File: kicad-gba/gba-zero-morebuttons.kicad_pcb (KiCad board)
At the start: 2 copper layers, 130.7 x 72.9 mm, 71 parts, among them J1 SWTCHCRFT_3.5JACK5-JACK-SMD, P1 50_PIN_CON, P3 LINK_CONNECTOR, Q1 BSS138, U1 APX803, U2 NC7WZ16, U3 74LVC2G02, U4 74LVC3G04, U5 LM4875, U6 RPI-ZEROSMD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

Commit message: fixed major issue
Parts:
- removed REF**: Val**, gba-zero-morebuttons:XY_BUTTON
- added S7: XY_BUTTON, gba-zero-morebuttons:XY_BUTTON, F.Cu at (200.1, 97.6)
- P2: value (none) -> JST_2PIN
- S5: value Val** -> AB_BUTTON
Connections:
- net AUD_PWM renamed /AUD_PWM
- net BAT renamed Net-(P2-2)
- net BKLT renamed /BKLT
- net BKLT_PWM renamed /BKLT_PWM
- net BTN_A renamed /BTN_A
- net BTN_B renamed /BTN_B
- net BTN_D renamed /BTN_D
- net BTN_L renamed /BTN_L
- net BTN_LS renamed /BTN_LS
- net BTN_R renamed /BTN_R
- net BTN_RS renamed /BTN_RS
- net BTN_SEL renamed /BTN_SEL
- net BTN_STR renamed /BTN_STR
- net BTN_U renamed /BTN_U
- net BYPASS renamed Net-(C10-P$1)
- net LBO renamed /LBO
- net MISO renamed /MISO
- net MOSI renamed /MOSI
- net MOSI_3V renamed /MOSI_3V
- net PWR_EN_RPI renamed /PWR_EN_RPI
- net PWR_SW_SEN renamed /PWR_SW_SEN
- net RING renamed Net-(C13-P$2)
- net RT_INT renamed /RT_INT
- net RXD renamed /RXD
- net SCL renamed /SCL
- net SCLK renamed /SCLK
- net SCLK_3V renamed /SCLK_3V
- net SDA renamed /SDA
- net SENSE renamed Net-(U5-SENSE)
- net TFT_CS_3V renamed /TFT_CS_3V
- net TFT_DC_3V renamed /TFT_DC_3V
- net TFT_RST renamed /TFT_RST
- net TXD renamed /TXD
- net USB renamed /USB
- net VO1 renamed Net-(C13-P$1)
- net VO2 renamed Net-(SP1--)
- net VOL/SD renamed Net-(U5-VOL/~{SD})
- J1 pad 4: (no net) -> unconnected-(J1-Pad4)
- P1 pad 11: (no net) -> unconnected-(P1-VSYNC-Pad11)
- P1 pad 12: (no net) -> unconnected-(P1-HSYNC-Pad12)
- P1 pad 13: (no net) -> unconnected-(P1-DOTCLK-Pad13)
- P1 pad 14: (no net) -> unconnected-(P1-DE-Pad14)
- P1 pad 35: (no net) -> unconnected-(P1-/RD-Pad35)
- P1 pad 39: (no net) -> unconnected-(P1-TE-Pad39)
- R17 pad 2O: (no net) -> unconnected-(R17-Pad2O)
- U2 pad 3: (no net) -> unconnected-(U2-A2-Pad3)
- U2 pad 4: (no net) -> unconnected-(U2-Y2-Pad4)
- U6 pad 31: (no net) -> /BTN_X
- U6 pad 35: (no net) -> /BTN_Y
- U7 pad VS: (no net) -> unconnected-(U7-PadVS)
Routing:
- net (no net): track 78.7 -> 0.00 mm, vias 2 -> 0
- net /BTN_X: track 0.00 -> 43.5 mm, vias 0 -> 1
- net /BTN_Y: track 0.00 -> 42.4 mm, vias 0 -> 1
- net BTN_Y: track 3.77 -> 0.00 mm
- net BTN_X: track 3.73 -> 0.00 mm

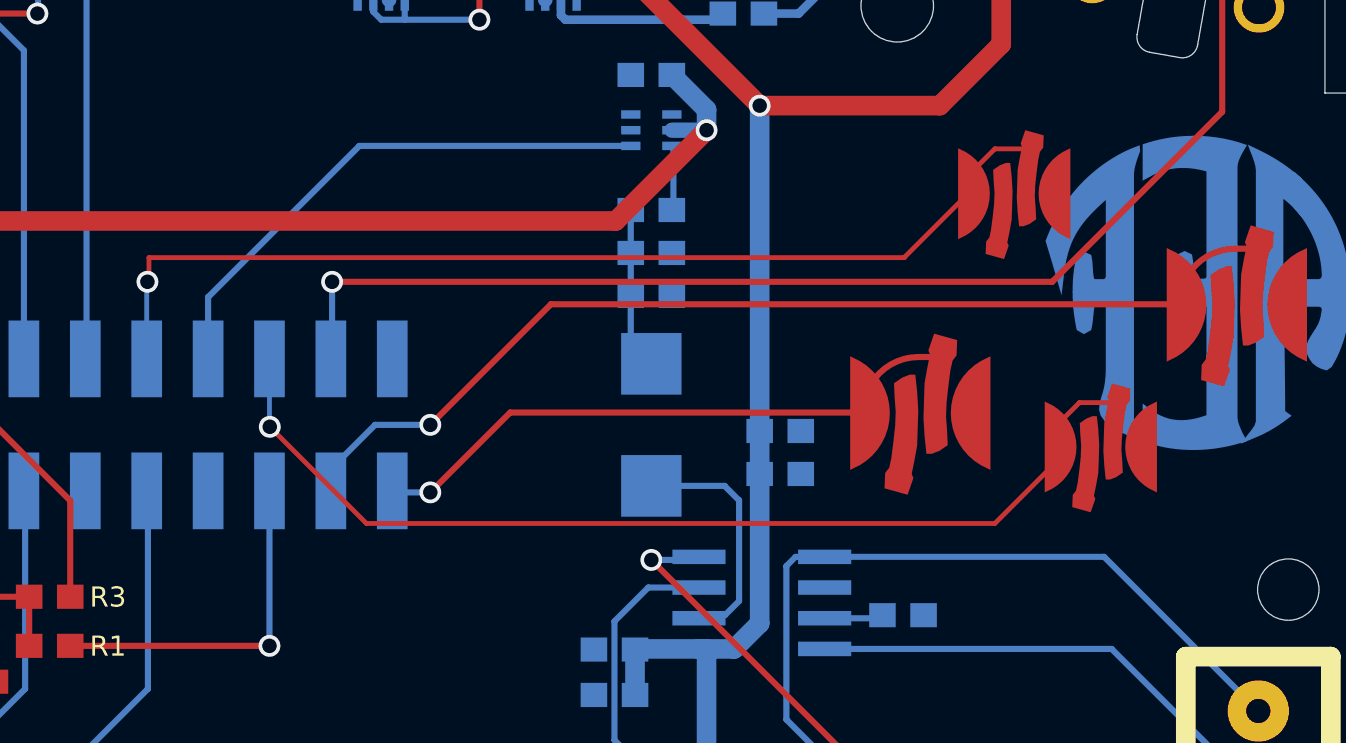
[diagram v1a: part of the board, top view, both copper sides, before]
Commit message: final update of button position
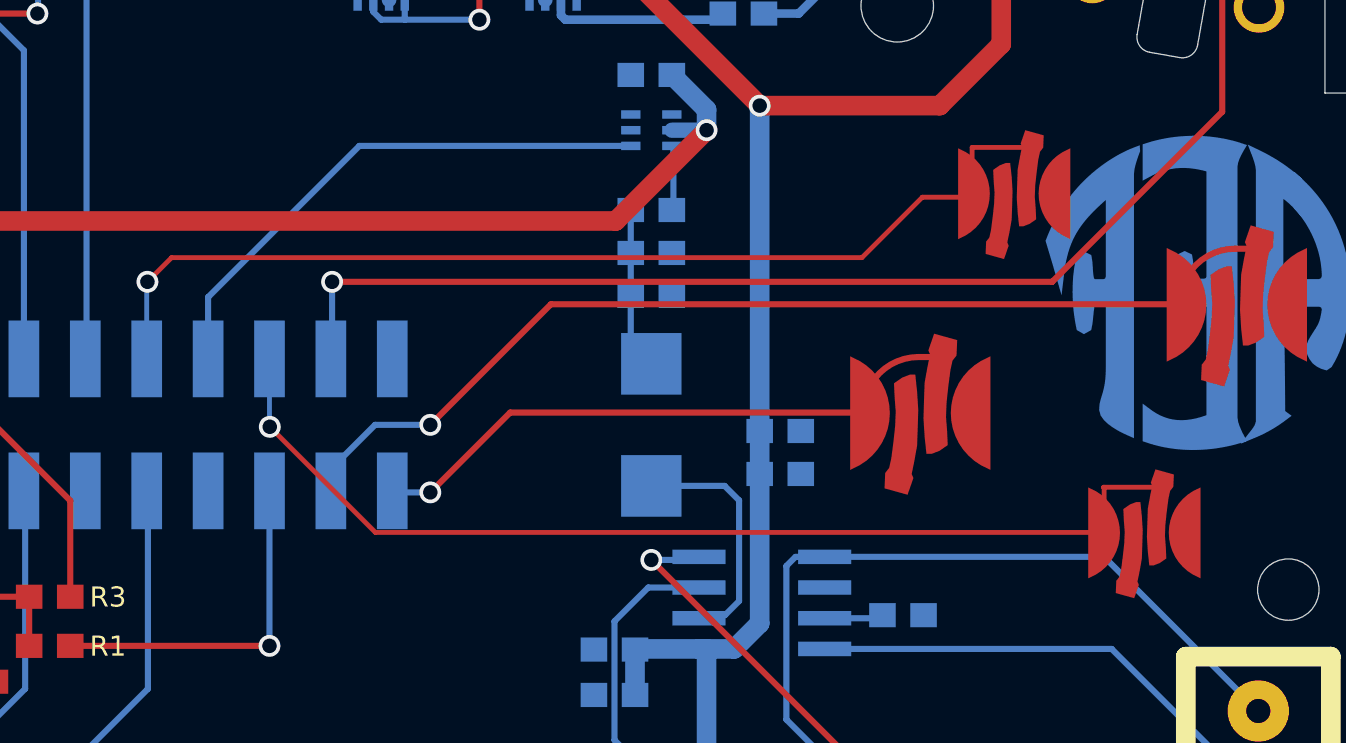
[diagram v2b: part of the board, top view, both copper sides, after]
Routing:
- net /BTN_Y: track 42.4 -> 43.4 mm
